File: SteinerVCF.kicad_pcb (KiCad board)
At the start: 2 copper layers, 39.6 x 100 mm, 72 parts, among them J1 AudioJack2_Ground_Switch, J2 AudioJack2_Ground_Switch, J3 AudioJack2_Ground_Switch, J4 AudioJack2_Ground_Switch, J5 AudioJack2_Ground_Switch, J6 AudioJack2_Ground_Switch, J7 Conn_02x05_Odd_Even, J8 AudioJack2_Ground_Switch, J9 AudioJack2_Ground_Switch, Q1 BC847, Q2 BC847, U1 TL074

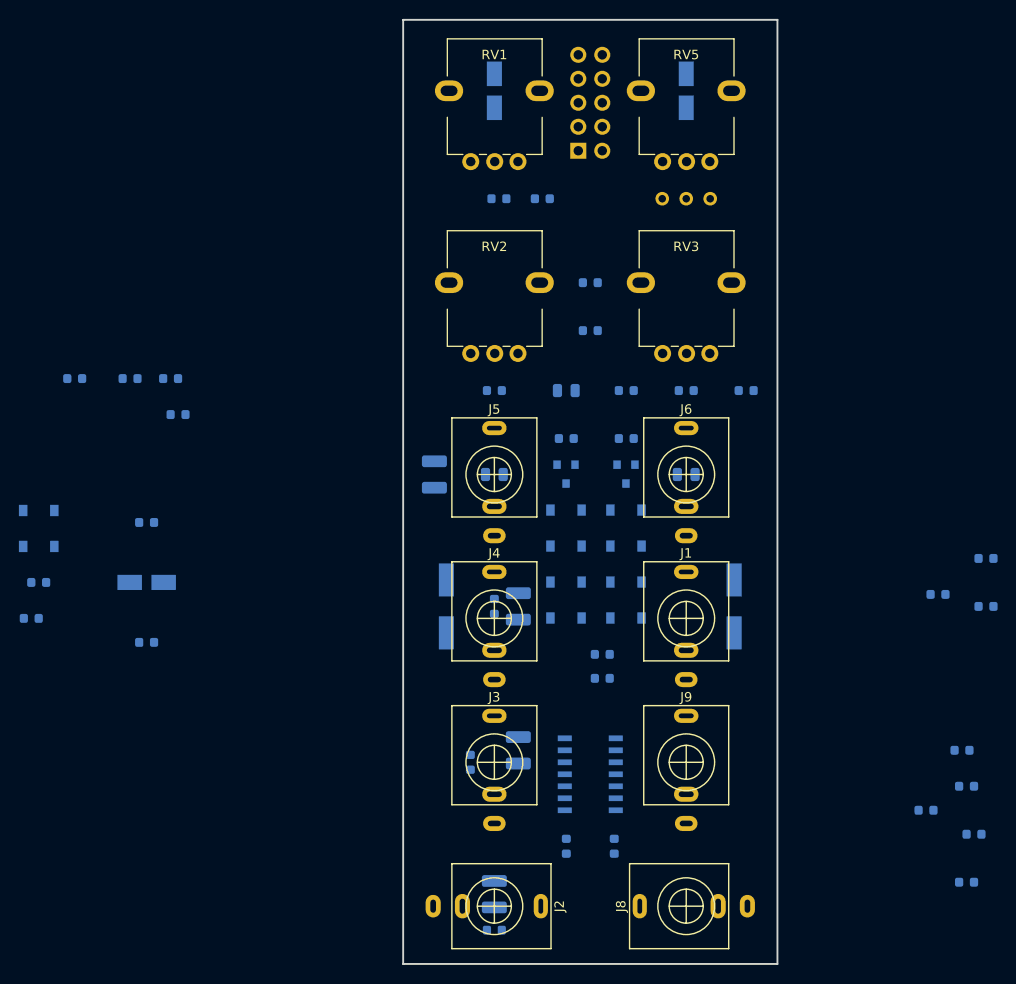
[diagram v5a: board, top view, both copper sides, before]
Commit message: Full-board placement complete.
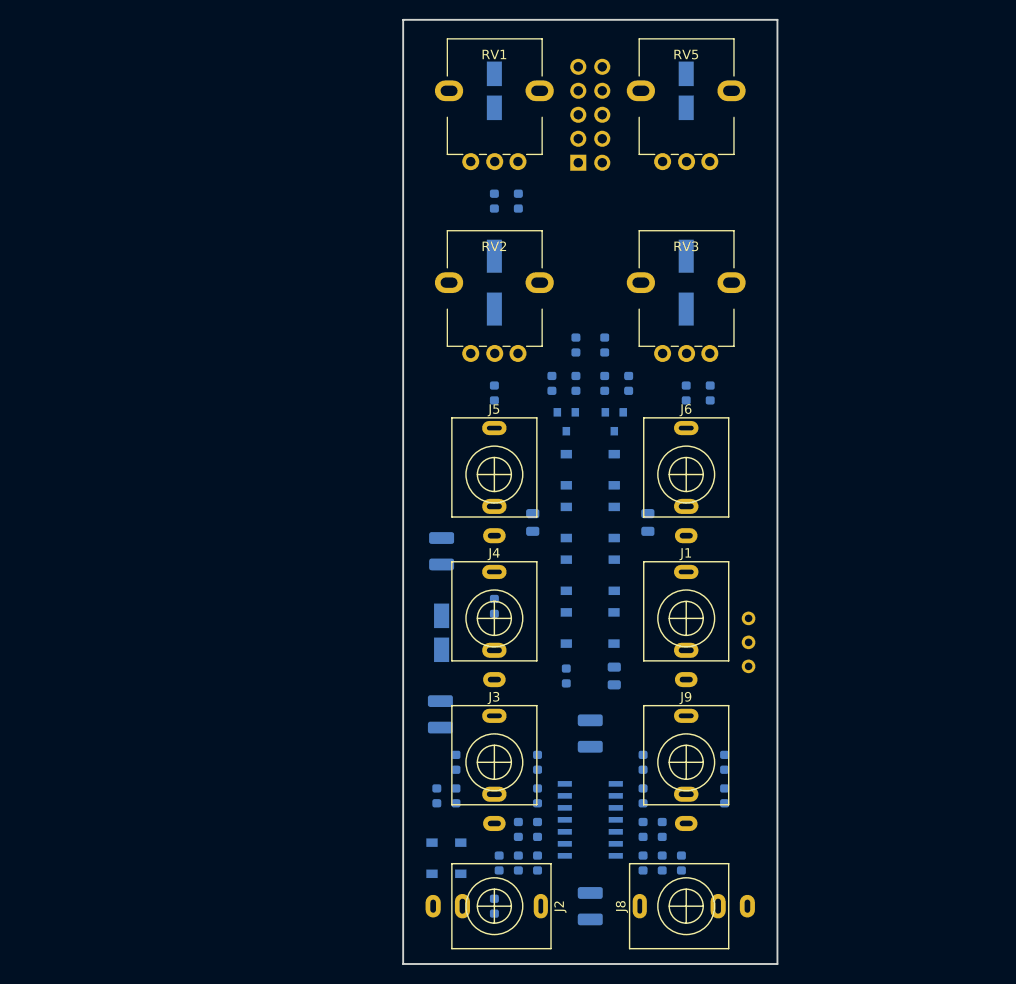
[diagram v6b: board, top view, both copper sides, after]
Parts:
- moved R16 68.6 mm to (162.7, 135.5), turned to 270 degrees
- moved R22 63.7 mm to (142.9, 135.5), turned to 270 degrees
- moved R19 61.8 mm to (142.9, 139.0), turned to 270 degrees
- moved R25 59.6 mm to (142.9, 146.1), turned to 90 degrees
- moved C15 58.9 mm to (140.9, 146.1), turned to 90 degrees
- moved D9 55.6 mm to (131.7, 145.6), turned to 270 degrees
- moved D10 55.6 mm to (134.8, 145.6), turned to 90 degrees
- moved R18 53.5 mm to (134.3, 139.0), turned to 90 degrees
- moved R26 49.5 mm to (138.8, 146.1), turned to 270 degrees
- moved RV4 45.4 mm to (165.3, 120.2), turned to 90 degrees
- moved R24 44.1 mm to (140.9, 142.6), turned to 90 degrees
- moved R17 42.3 mm to (154.1, 135.5), turned to 90 degrees
- moved R23 42.2 mm to (132.2, 139.0), turned to 90 degrees
- moved R20 37.8 mm to (154.1, 139.0), turned to 90 degrees
- moved R28 35.2 mm to (154.1, 146.1), turned to 90 degrees
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
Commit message: Completed signal routing.
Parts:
- moved C1 47.9 mm to (132.8, 105.5)
- moved RV4 17.8 mm to (165.3, 102.5)
- moved R1 10.4 mm to (133.5, 68.7), turned to 90 degrees
- moved R16 6.60 mm to (156.1, 135.5)
- moved R18 6.60 mm to (140.9, 139.0)
- moved R21 6.60 mm to (156.1, 139.0)
- moved R6 6.60 mm to (140.9, 135.5)
- moved R14 5.75 mm to (146.0, 91.3)
- moved R11 5.40 mm to (153.6, 95.3)
- moved R10 4.06 mm to (151.0, 91.3)
- moved R15 1.52 mm to (151.0, 95.3)
- moved C5 1.02 mm to (152.1, 126.3)
- moved D1 1.02 mm to (144.9, 104.5)
- moved D2 1.02 mm to (144.9, 110.1)
- moved D3 1.02 mm to (144.9, 115.7)
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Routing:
- net +12V: track 0.00 -> 129.4 mm
- net Net-(R17-Pad1): track 0.00 -> 100.4 mm
- net /Resonance: track 0.00 -> 97.9 mm
- net -12V: track 0.00 -> 91.2 mm
- net Net-(Q1-Pad1): track 0.00 -> 87.1 mm, vias 0 -> 2
- net Net-(C2-Pad1): track 0.00 -> 73.3 mm, vias 0 -> 4
- net Net-(C1-Pad2): track 0.00 -> 53.4 mm
- net Net-(C12-Pad1): track 0.00 -> 37.4 mm
- net LoopOut: track 0.00 -> 33.0 mm, vias 0 -> 2
- net Net-(C1-Pad1): track 0.00 -> 29.7 mm, vias 0 -> 2
- net Net-(C3-Pad1): track 0.00 -> 29.1 mm, vias 0 -> 2
- net LoopIn: track 0.00 -> 27.1 mm
- net Net-(C16-Pad2): track 0.00 -> 20.4 mm
- net Net-(C7-Pad1): track 0.00 -> 19.8 mm
- net Net-(C15-Pad2): track 0.00 -> 19.7 mm
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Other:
- rule trace_min: 0.2 -> 0.25

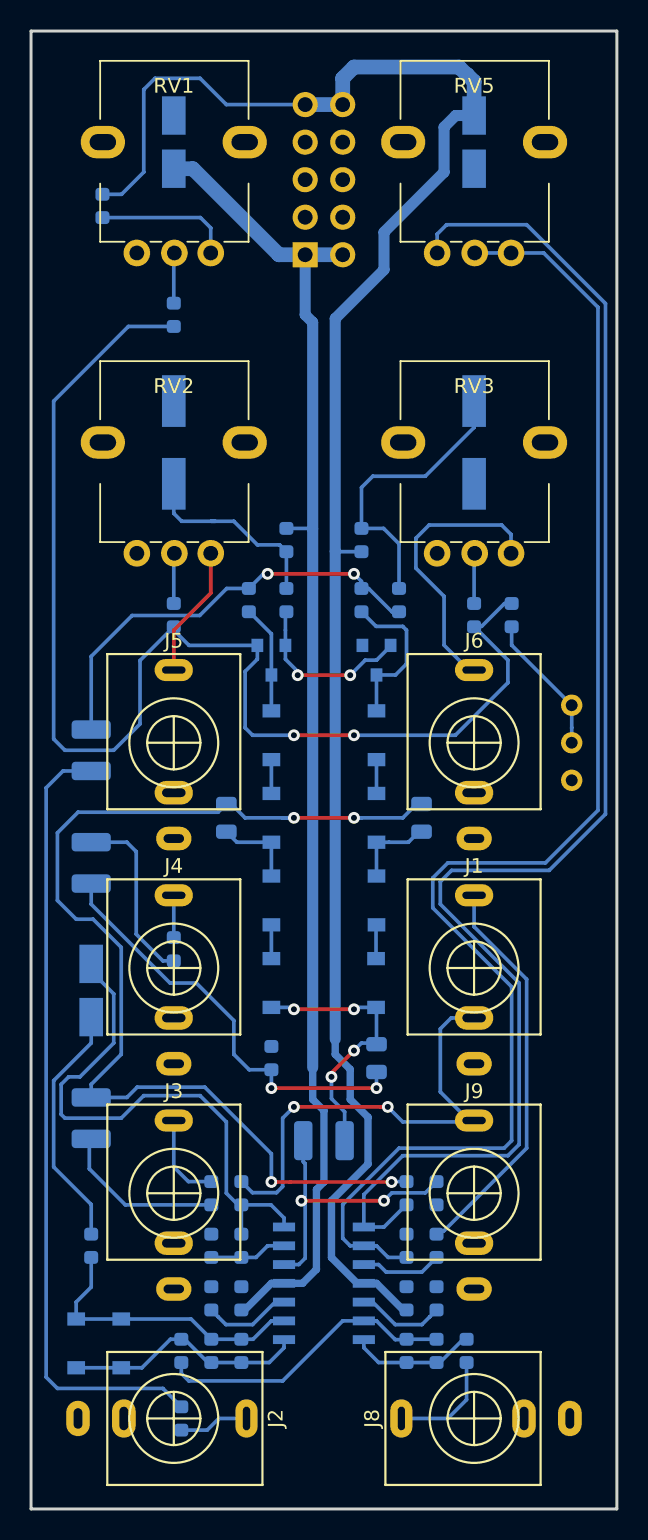
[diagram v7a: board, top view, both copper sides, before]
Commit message: Ground pours and stiching.
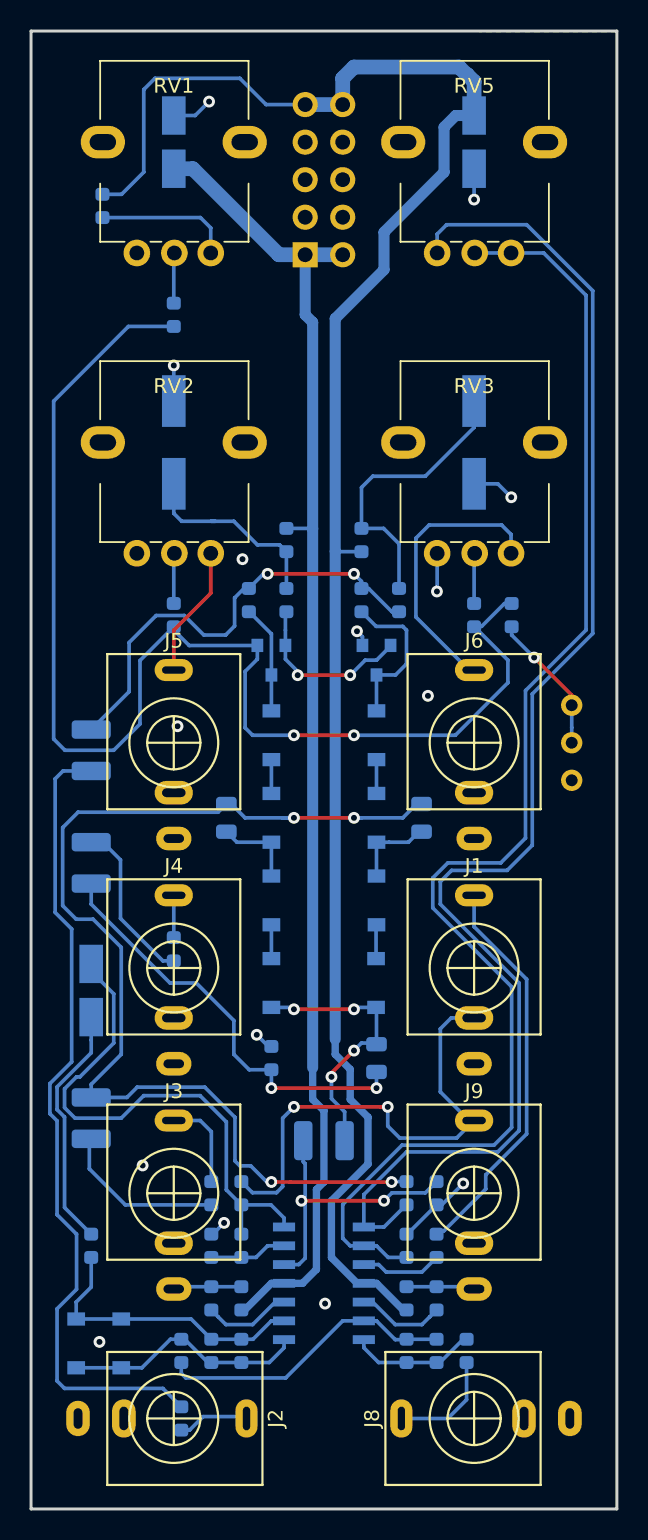
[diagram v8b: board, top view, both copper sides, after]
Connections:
- C10 pad 2: (no net) -> GND
- C11 pad 1: (no net) -> GND
- C13 pad 2: (no net) -> GND
- C14 pad 1: (no net) -> GND
- C6 pad 1: (no net) -> GND
- C7 pad 2: (no net) -> GND
- J1 pad S: (no net) -> GND
- J2 pad S: (no net) -> GND
- J3 pad S: (no net) -> GND
- J4 pad S: (no net) -> GND
- J5 pad S: (no net) -> GND
- J6 pad S: (no net) -> GND
- J7 pad 3: (no net) -> GND
- J7 pad 4: (no net) -> GND
- J7 pad 5: (no net) -> GND
- J7 pad 6: (no net) -> GND
- J7 pad 7: (no net) -> GND
- J7 pad 8: (no net) -> GND
- J8 pad S: (no net) -> GND
- J9 pad S: (no net) -> GND
- Q2 pad 1: (no net) -> GND
- R12 pad 2: (no net) -> GND
- R16 pad 2: (no net) -> GND
- R18 pad 2: (no net) -> GND
- R20 pad 2: (no net) -> GND
- R24 pad 2: (no net) -> GND
- R27 pad 2: (no net) -> GND
- RV1 pad 3: (no net) -> GND
- RV2 pad 3: (no net) -> GND
- RV3 pad 3: (no net) -> GND
- RV4 pad 3: (no net) -> GND
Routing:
- net GND: track 0.00 -> 30.9 mm, vias 0 -> 15
- net /Resonance: track 97.9 -> 94.9 mm
- net Net-(R17-Pad1): track 100.4 -> 97.4 mm
- net LoopOut: track 33.0 -> 34.7 mm
- net Net-(C1-Pad2): track 53.4 -> 54.9 mm
- net Net-(C1-Pad1): track 29.7 -> 30.9 mm
- net Net-(C12-Pad1): track 37.4 -> 36.4 mm
- net Net-(C3-Pad2): track 12.2 -> 11.2 mm
- net Net-(R9-Pad2): vias 0 -> 1
- added copper zone on B.Cu, net GND
- added copper zone on F.Cu, net GND
